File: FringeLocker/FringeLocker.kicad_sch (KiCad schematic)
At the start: 17 parts, among them J1 OUT, J2 PWR, U1 TL072

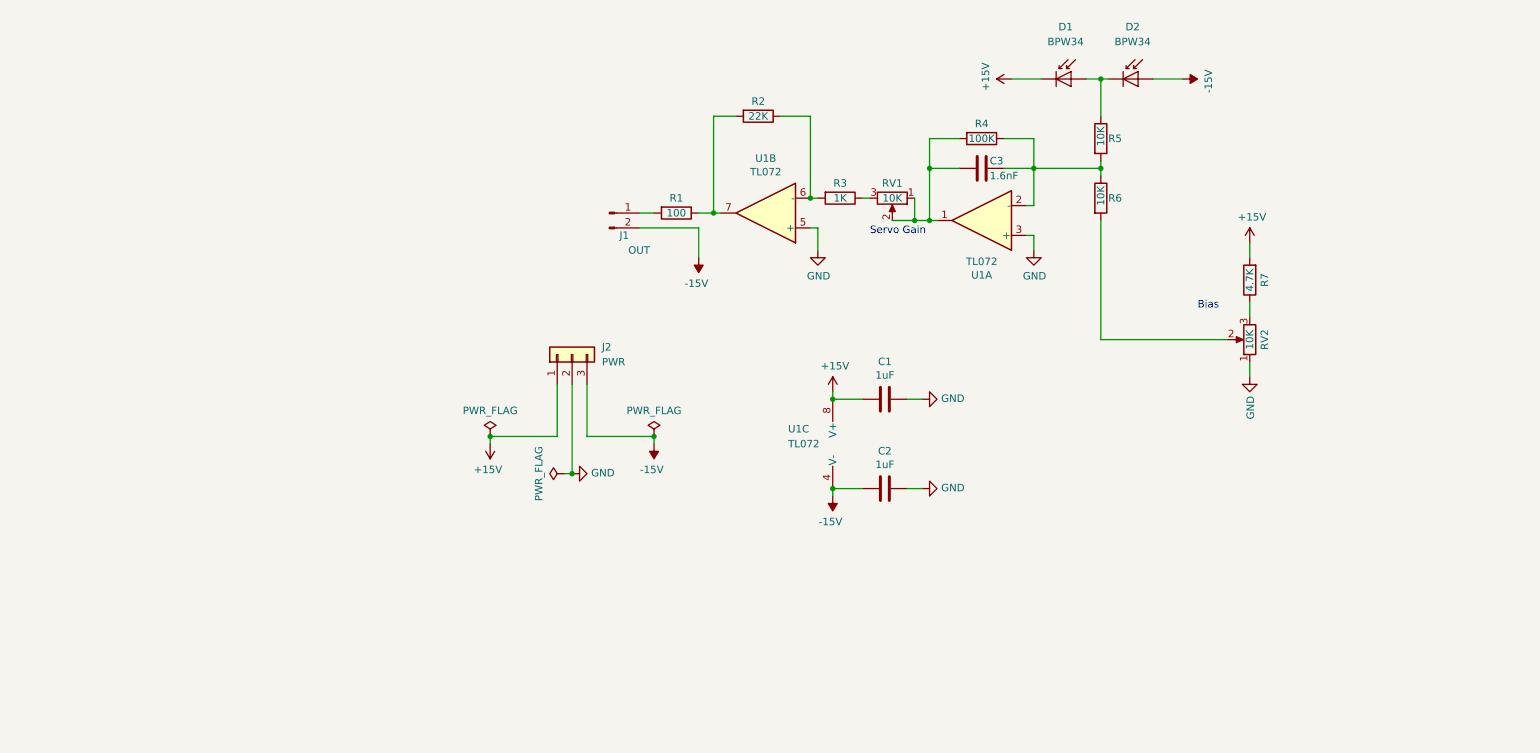
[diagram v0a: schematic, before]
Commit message: Added 23A PSU
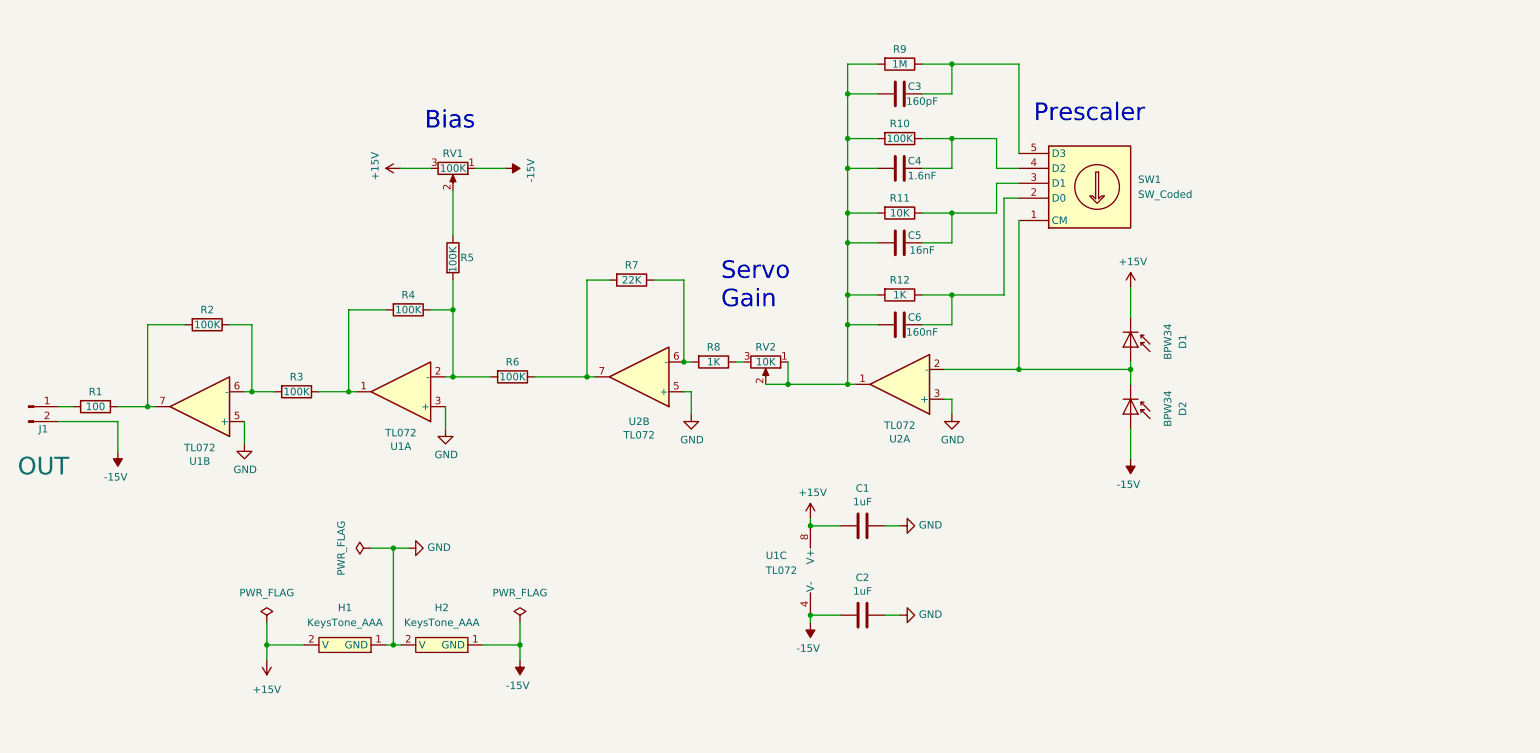
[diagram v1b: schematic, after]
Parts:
- removed J2: PWR, Connector_PinHeader_2.54mm:PinHeader_1x03_P2.54mm_Vertical, symbol Connector_Generic:Conn_01x03
- removed R5: 10K, Resistor_THT:R_Axial_DIN0207_L6.3mm_D2.5mm_P10.16mm_Horizontal, symbol Device:R
- removed R7: 4.7K, Resistor_THT:R_Axial_DIN0207_L6.3mm_D2.5mm_P10.16mm_Horizontal, symbol Device:R
- added C4: 1.6nF, Capacitor_THT:CP_Radial_Tantal_D4.5mm_P5.00mm, symbol Device:C
- added C5: 16nF, Capacitor_THT:CP_Radial_Tantal_D4.5mm_P5.00mm, symbol Device:C
- added C6: 160nF, Capacitor_THT:CP_Radial_Tantal_D4.5mm_P5.00mm, symbol Device:C
- added H1, H2: KeysTone_AAA, symbol My_Library:KeysTone_AAA
- added R10, R2, R3, R4, R6: 100K, Resistor_THT:R_Axial_DIN0207_L6.3mm_D2.5mm_P10.16mm_Horizontal, symbol Device:R
- added R11: 10K, Resistor_THT:R_Axial_DIN0207_L6.3mm_D2.5mm_P10.16mm_Horizontal, symbol Device:R
- added R12: 1K, Resistor_THT:R_Axial_DIN0207_L6.3mm_D2.5mm_P10.16mm_Horizontal, symbol Device:R
- added SW1: SW_Coded, symbol Switch:SW_Coded
- added unit 2 of U1
- added unit 1 of U1
- C3: value 1.6nF -> 160pF
- R5: renamed from R6; value 10K -> 100K
- R9: renamed from R4; value 100K -> 1M
- RV1: renamed from RV2; value 10K -> 100K
- renumbered R2 to R7, R3 to R8, RV1 to RV2, U1 to U2
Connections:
- net +15V: now also RV1.3, H1.2 (V)
- net -15V: now also RV1.1, H2.1 (GND)
- net GND: now also H1.1 (GND), H2.2 (V), U1.3 (+), U1.5 (+); no longer RV1.1
- net at C3.1, R9.2, RV2.1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: now also C4.1, C5.1, C6.1, R10.2, R11.2, R12.2
- net at C3.2, R9.1: now also SW1.5 (D3); no longer R5.1, U2.2 (-)
- net at D1.2 (A), D2.1 (K): now also U2.2 (-), SW1.1 (CM)
- net at R7.2, U2.7: now also R6.1; no longer R1.1
- net at RV1.2: now also R5.1; no longer R5.2
- new net: R1.1, R2.2, U1.7
- new net: R4.1, R5.2, R6.2, U1.2 (-)
- new net: C4.2, R10.1, SW1.4 (D2)
- new net: R2.1, R3.2, U1.6 (-)
- new net: C6.2, R12.1, SW1.2 (D0)
- new net: R3.1, R4.2, U1.1
- new net: C5.2, R11.1, SW1.3 (D1)
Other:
- note added: "Prescaler"
- moved on the sheet: C2, C3, D1, D2, J1, R1, R5, R7, R8, R9, RV1, RV2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

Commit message: V1.0
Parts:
- removed H1, H2: KeysTone_AAA, symbol My_Library:KeysTone_AAA
- removed R4, R5, R6: 100K, Resistor_THT:R_Axial_DIN0207_L6.3mm_D2.5mm_P10.16mm_Horizontal, symbol Device:R
- removed SW1: SW_Coded, symbol Switch:SW_Coded
- removed U1, U2: TL072, Package_SO:SOIC-8_3.9x4.9mm_P1.27mm, symbol Amplifier_Operational:TL072
- added BH1, BH2: KeysTone_AAA, BatteryHolder:Keystone_AAA, symbol My_Library:KeysTone_AAA
- added D3: LED_Small, LED_SMD:LED_0402_1005Metric_Pad0.77x0.64mm_HandSolder, symbol Device:LED_Small
- added J2: TP Scaler, Connector_PinHeader_2.54mm:PinHeader_1x02_P2.54mm_Vertical, symbol Connector:Conn_01x02_Male
- added J3: Conn_01x03_Male, Connector_PinHeader_2.54mm:PinHeader_1x03_P2.54mm_Vertical, symbol Connector:Conn_01x03_Male
- added R10: 10K, Resistor_SMD:R_0805_2012Metric_Pad1.20x1.40mm_HandSolder, symbol Device:R
- added SW1: NIDEC_SS-10-16, BatteryHolder:NIDEC_SS-10-16, symbol My_Library:NIDEC_SS-10-16
- added SW2: SW_Push_DPDT, BatteryHolder:SlideSwitchASE_DPDT, symbol Switch:SW_Push_DPDT
- added TP1: TP OUT, TestPoint:TestPoint_THTPad_D1.0mm_Drill0.5mm, symbol Connector:TestPoint
- added TP2: TP Bias, TestPoint:TestPoint_THTPad_D1.0mm_Drill0.5mm, symbol Connector:TestPoint
- added TP3: TP PDs, TestPoint:TestPoint_THTPad_D1.0mm_Drill0.5mm, symbol Connector:TestPoint
- added U1: TL074, Package_SO:SO-14_5.3x10.2mm_P1.27mm, symbol Amplifier_Operational:TL074
- C1: renamed from C3; footprint Capacitor_THT:CP_Radial_Tantal_D4.5mm_P5.00mm -> Capacitor_SMD:C_0603_1608Metric_Pad1.08x0.95mm_HandSolder
- C2: renamed from C4; footprint Capacitor_THT:CP_Radial_Tantal_D4.5mm_P5.00mm -> Capacitor_SMD:C_0603_1608Metric_Pad1.08x0.95mm_HandSolder
- C3: renamed from C5; footprint Capacitor_THT:CP_Radial_Tantal_D4.5mm_P5.00mm -> Capacitor_SMD:C_0603_1608Metric_Pad1.08x0.95mm_HandSolder
- C4: renamed from C6; footprint Capacitor_THT:CP_Radial_Tantal_D4.5mm_P5.00mm -> Capacitor_SMD:C_0603_1608Metric_Pad1.08x0.95mm_HandSolder
- C5: renamed from C1; footprint Capacitor_THT:CP_Radial_D5.0mm_P2.00mm -> Capacitor_SMD:C_0603_1608Metric_Pad1.08x0.95mm_HandSolder
- C6: renamed from C2; footprint Capacitor_THT:CP_Radial_D5.0mm_P2.00mm -> Capacitor_SMD:C_0603_1608Metric_Pad1.08x0.95mm_HandSolder
- R1: footprint Resistor_THT:R_Axial_DIN0207_L6.3mm_D2.5mm_P10.16mm_Horizontal -> Resistor_SMD:R_0805_2012Metric_Pad1.20x1.40mm_HandSolder
- R2: renamed from R7; footprint Resistor_THT:R_Axial_DIN0207_L6.3mm_D2.5mm_P10.16mm_Horizontal -> Resistor_SMD:R_0805_2012Metric_Pad1.20x1.40mm_HandSolder
- R3: renamed from R2; footprint Resistor_THT:R_Axial_DIN0207_L6.3mm_D2.5mm_P10.16mm_Horizontal -> Resistor_SMD:R_0805_2012Metric_Pad1.20x1.40mm_HandSolder
- R4: renamed from R8; footprint Resistor_THT:R_Axial_DIN0207_L6.3mm_D2.5mm_P10.16mm_Horizontal -> Resistor_SMD:R_0805_2012Metric_Pad1.20x1.40mm_HandSolder
- R5: renamed from R3; footprint Resistor_THT:R_Axial_DIN0207_L6.3mm_D2.5mm_P10.16mm_Horizontal -> Resistor_SMD:R_0805_2012Metric_Pad1.20x1.40mm_HandSolder
- R6: renamed from R9; footprint Resistor_THT:R_Axial_DIN0207_L6.3mm_D2.5mm_P10.16mm_Horizontal -> Resistor_SMD:R_0805_2012Metric_Pad1.20x1.40mm_HandSolder
- R7: renamed from R10; footprint Resistor_THT:R_Axial_DIN0207_L6.3mm_D2.5mm_P10.16mm_Horizontal -> Resistor_SMD:R_0805_2012Metric_Pad1.20x1.40mm_HandSolder
- R8: renamed from R11; footprint Resistor_THT:R_Axial_DIN0207_L6.3mm_D2.5mm_P10.16mm_Horizontal -> Resistor_SMD:R_0805_2012Metric_Pad1.20x1.40mm_HandSolder
- R9: renamed from R12; footprint Resistor_THT:R_Axial_DIN0207_L6.3mm_D2.5mm_P10.16mm_Horizontal -> Resistor_SMD:R_0805_2012Metric_Pad1.20x1.40mm_HandSolder
- RV1: renamed from RV2; footprint Potentiometer_THT:Potentiometer_Bourns_3386F_Vertical -> Potentiometer_THT:Potentiometer_Bourns_3266W_Vertical
- RV2: renamed from RV1; footprint Potentiometer_THT:Potentiometer_Bourns_3386F_Vertical -> Potentiometer_THT:Potentiometer_Bourns_3266W_Vertical
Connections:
- net +15V: now also R10.1, SW2.3 (C), U1.4 (V+)
- net -15V: now also SW2.6 (C), U1.11 (V-); no longer J1.2 (Pin_2)
- net GND: now also BH1.3 (GND), BH1.4 (GND), BH2.1 (V), BH2.2 (V), D3.1 (K), J2.2 (Pin_2), J3.2 (Pin_2), U1.10 (+), U1.3 (+), U1.5 (+)
- net at C1.1, C2.1, C3.1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: now also J2.1 (Pin_1), U1.1
- net at D1.2 (A), D2.1 (K): now also SW1.2 (C), TP3.1, U1.2 (-)
- net at R2.1, R4.2: now also U1.6 (-)
- net at R2.2: now also R1.1, TP1.1, U1.7
- net at R3.2: now also J1.2 (Pin_2), TP2.1, U1.8; no longer R1.1
- net at C1.2, R6.1: now also SW1.8 (1)
- net at RV2.2: now also R5.1
- net at C2.2, R7.1: now also SW1.6 (2)
- net at R3.1, R5.2: now also U1.9 (-)
- net at C4.2, R9.1: now also SW1.4
- net at C3.2, R8.1: now also SW1.5 (3)
- new net: D3.2 (A), R10.2
- new net: BH1.1 (V), BH1.2 (V), J3.1 (Pin_1), SW2.2 (B)
- new net: BH2.3 (GND), BH2.4 (GND), J3.3 (Pin_3), SW2.5 (B)
- no-connect marks 0 -> 8
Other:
- note added: "Auxiliary PSU"
- moved on the sheet: C1, C2, C3, C4, C5, C6, D1, D2, J1, R1, R2, R3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
